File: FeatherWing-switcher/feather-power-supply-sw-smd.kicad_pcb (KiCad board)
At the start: 2 copper layers, 9 parts, among them J4 QWIIC, J5 0.1, Q1 Q_PMOS_GSD

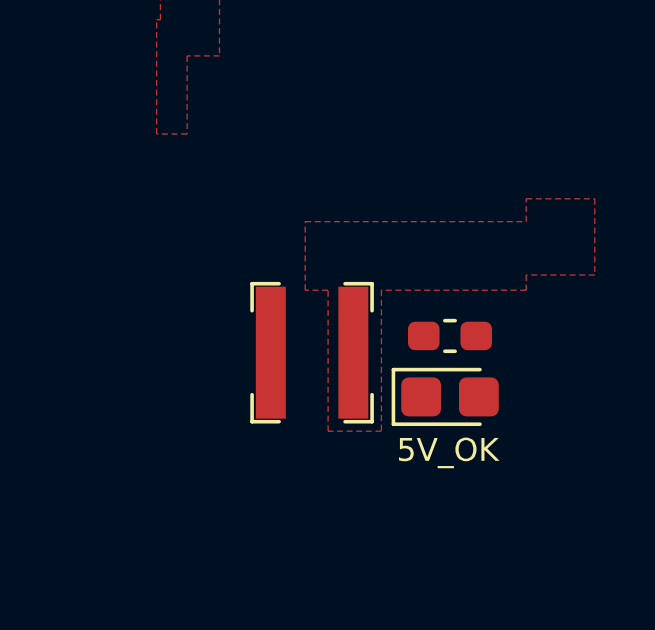
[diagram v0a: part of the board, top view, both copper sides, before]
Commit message: fixes 5V bodge and connects vdivider
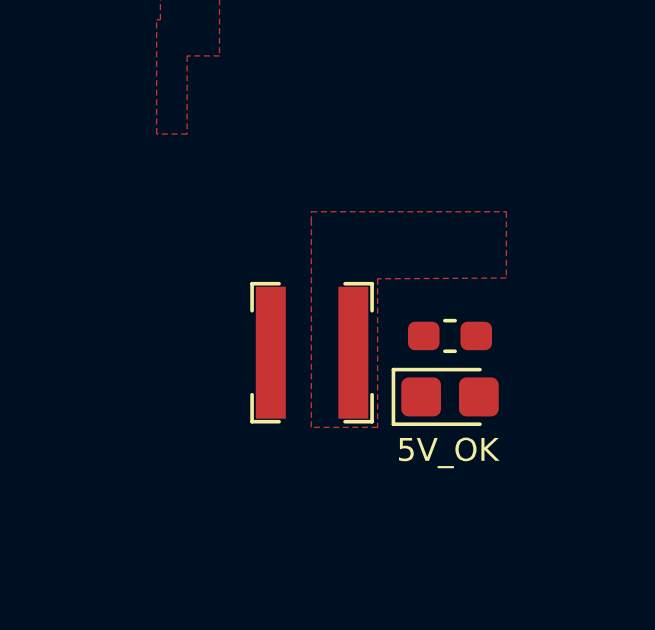
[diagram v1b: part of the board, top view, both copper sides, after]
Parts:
- removed REF**: KiCad-Logo2_5mm_SilkScreen, Symbol:KiCad-Logo2_5mm_SilkScreen
